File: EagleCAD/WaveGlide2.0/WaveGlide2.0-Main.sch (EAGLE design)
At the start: 47 parts, among them CN3 0, IC1 MC33502D, K2 MS-20-310-HN, Q2 reset, U1 ATMEGA328P_TQFP, U2 BMP180, U3 MPXV7002, U4 TPS55340PWP, U5 UG-2828GDEDF11, Y2 12MHz

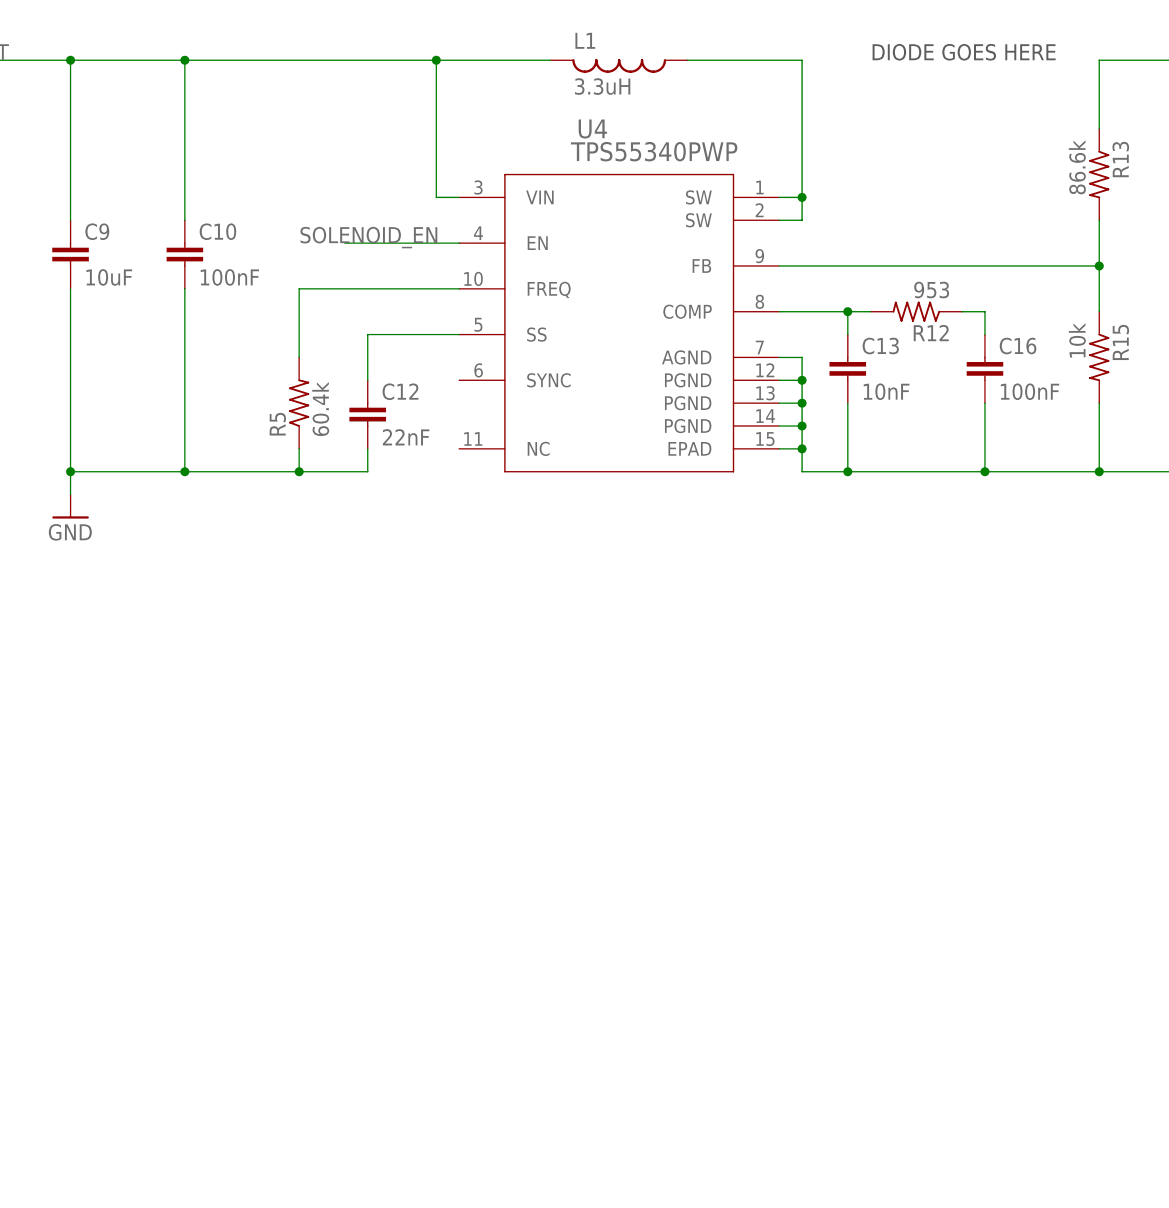
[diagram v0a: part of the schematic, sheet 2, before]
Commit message: Add 5V regulator
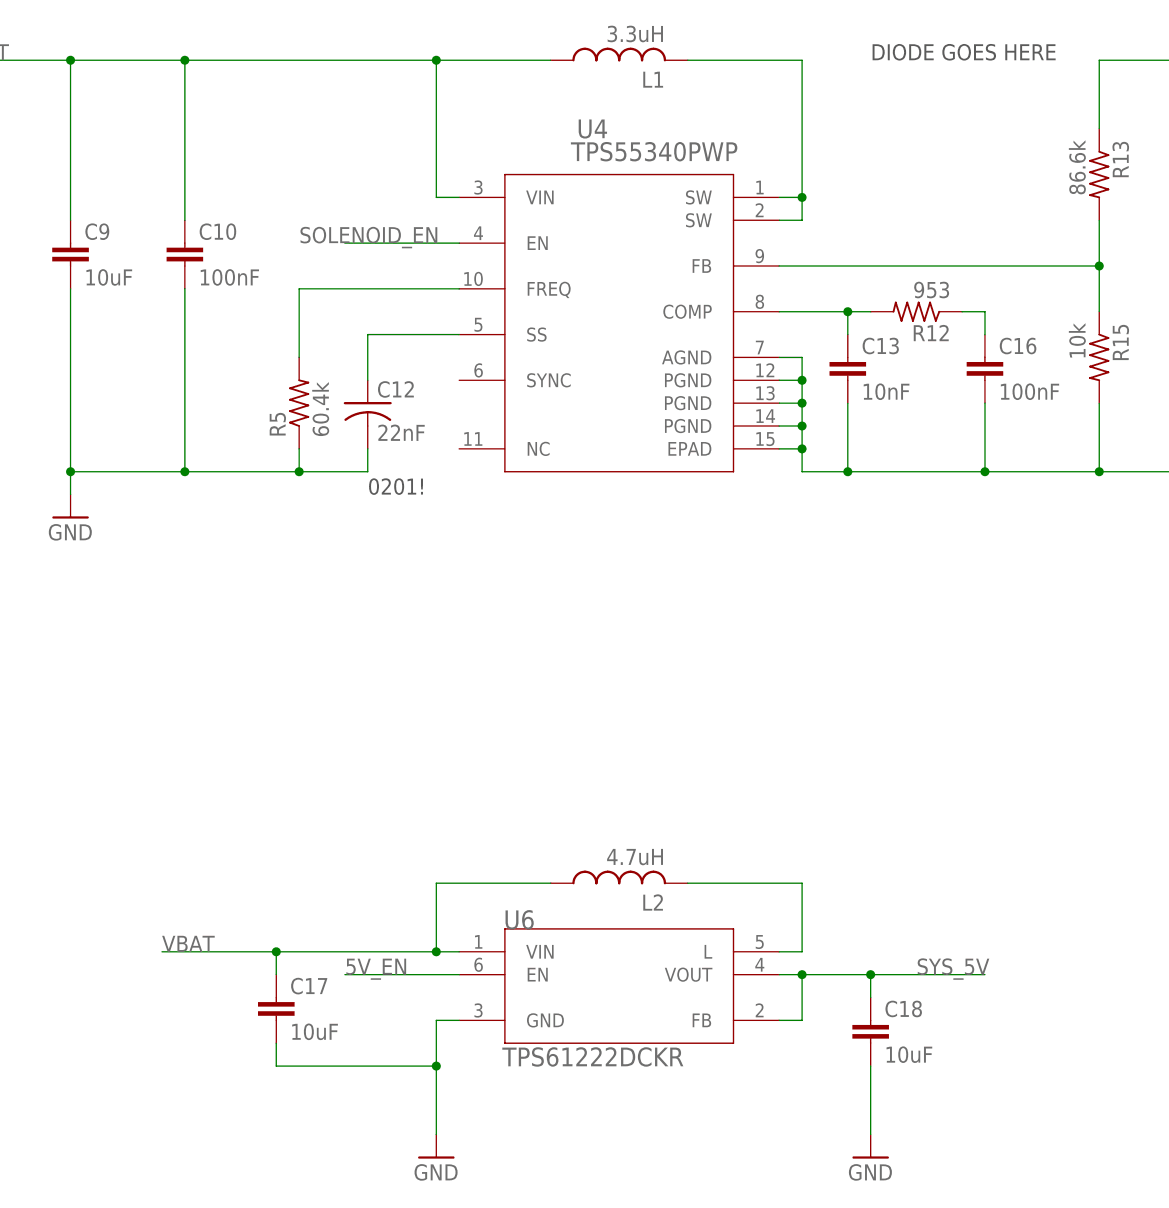
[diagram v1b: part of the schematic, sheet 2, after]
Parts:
- added C17, C18: 10uF, resistor:C-EUC0805
- added L2: 4.7uH, resistor:L-USL2825P
- added U6: TPS61222DCKR, CustomParts:TPS61222DCKR
- C12: device resistor:C-EUC0805 -> resistor:C-USC0201
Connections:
- new net 5V_EN: U6.EN
- new net N$6: L2.2, U6.L
- net GND: now also C17.2, C18.2, U6.GND
- net SYS_5V: now also C18.1, U6.FB, U6.VOUT
- net TPS55340_SW: now also L1.2; no longer L1.1
- net VBAT: now also C17.1, L1.1, L2.1, U6.VIN; no longer L1.2
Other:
- note added: "0201!"
- moved on the sheet: L1
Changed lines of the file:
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@@
 <?xml version="1.0" encoding="utf-8"?>
 <!DOCTYPE eagle SYSTEM "eagle.dtd">
-<eagle version="8.7.0">
+<eagle version="8.7.1">
 <drawing>
 <settings>
@@
 <attribute name="POPULATE" value="1"/>
 </part>
-<part name="C12" library="resistor" library_urn="urn:adsk.eagle:library:348" deviceset="C-EU" device="C0805" package3d_urn="urn:adsk.eagle:package:26137/1" value="22nF">
+<part name="C12" library="resistor" library_urn="urn:adsk.eagle:library:348" deviceset="C-US" device="C0201" package3d_urn="urn:adsk.eagle:package:26209/1" value="22nF">
 <attribute name="MPN" value="GRM033R60J223KE01D"/>
 <attribute name="POPULATE" value="1"/>
@@
 <attribute name="POPULATE" value="1"/>
 </part>
-<part name="U4" library="CustomParts" library_urn="urn:adsk.eagle:library:2193978" deviceset="TPS55340PWP" device="" package3d_urn="urn:adsk.eagle:package:2335473/2"/>
+<part name="U4" library="CustomParts" library_urn="urn:adsk.eagle:library:2193978" deviceset="TPS55340PWP" device="" package3d_urn="urn:adsk.eagle:package:2335473/3"/>
 <part name="GND7" library="supply1" library_urn="urn:adsk.eagle:library:371" deviceset="GND" device=""/>
 <part name="GND8" library="supply1" library_urn="urn:adsk.eagle:library:371" deviceset="GND" device=""/>
+<part name="U6" library="CustomParts" library_urn="urn:adsk.eagle:library:2193978" deviceset="TPS61222DCKR" device="" package3d_urn="urn:adsk.eagle:package:2230384/2">
+<attribute name="POPULATE" value="1"/>
+</part>
+<part name="L2" library="resistor" library_urn="urn:adsk.eagle:library:348" deviceset="L-US" device="L2825P" package3d_urn="urn:adsk.eagle:package:25928/1" value="4.7uH">
+<attribute name="MPN" value="LQM2HPN4R7MGCL"/>
+<attribute name="POPULATE" value="1"/>
+</part>
+<part name="C17" library="resistor" library_urn="urn:adsk.eagle:library:348" deviceset="C-EU" device="C0805" package3d_urn="urn:adsk.eagle:package:26137/1" value="10uF">
+<attribute name="MPN" value="GRM21BR60J106ME19L"/>
+<attribute name="POPULATE" value="1"/>
+<attribute name="TOL" value="20%"/>
+<attribute name="VOLT" value="6.3V"/>
+</part>
+<part name="C18" library="resistor" library_urn="urn:adsk.eagle:library:348" deviceset="C-EU" device="C0805" package3d_urn="urn:adsk.eagle:package:26137/1" value="10uF">
+<attribute name="MPN" value="C0805C106K8PACTU"/>
+<attribute name="POPULATE" value="1"/>
+<attribute name="TOL" value="10%"/>
+<attribute name="VOLT" value="10V"/>
+</part>
+<part name="GND9" library="supply1" library_urn="urn:adsk.eagle:library:371" deviceset="GND" device=""/>
+<part name="GND10" library="supply1" library_urn="urn:adsk.eagle:library:371" deviceset="GND" device=""/>
 </parts>
 <sheets>
@@
 <plain>
 <text x="121.92" y="254" size="1.778" layer="97">DIODE GOES HERE</text>
+<text x="66.04" y="205.74" size="1.778" layer="97">0201!</text>
 </plain>
 <instances>
@@
 <attribute name="POPULATE" x="147.32" y="220.98" size="1.778" layer="96" display="off"/>
 </instance>
-<instance part="L1" gate="G$1" x="93.98" y="254" rot="R270">
-<attribute name="MPN" x="93.98" y="254" size="1.778" layer="96" rot="R270" display="off"/>
-<attribute name="POPULATE" x="93.98" y="254" size="1.778" layer="96" display="off"/>
+<instance part="L1" gate="G$1" x="93.98" y="254" rot="R90">
+<attribute name="MPN" x="93.98" y="254" size="1.778" layer="96" rot="R90" display="off"/>
+<attribute name="POPULATE" x="93.98" y="254" size="1.778" layer="96" rot="R180" display="off"/>
 </instance>
 <instance part="U4" gate="A" x="93.98" y="226.06"/>
 <instance part="GND7" gate="1" x="33.02" y="203.2"/>
 <instance part="GND8" gate="1" x="170.18" y="203.2"/>
+<instance part="U6" gate="A" x="93.98" y="149.86">
+<attribute name="POPULATE" x="93.98" y="149.86" size="1.778" layer="96" display="off"/>
+</instance>
+<instance part="L2" gate="G$1" x="93.98" y="162.56" rot="R90">
+<attribute name="MPN" x="93.98" y="162.56" size="1.778" layer="96" rot="R90" display="off"/>
+<attribute name="POPULATE" x="93.98" y="162.56" size="1.778" layer="96" rot="R90" display="off"/>
+</instance>
+<instance part="C17" gate="G$1" x="55.88" y="149.86">
+<attribute name="MPN" x="55.88" y="149.86" size="1.778" layer="96" rot="R270" display="off"/>
+<attribute name="POPULATE" x="55.88" y="149.86" size="1.778" layer="96" display="off"/>
+<attribute name="VOLT" x="55.88" y="149.86" size="1.778" layer="96" display="off"/>
+<attribute name="TOL" x="55.88" y="149.86" size="1.778" layer="96" display="off"/>
+</instance>
+<instance part="C18" gate="G$1" x="121.92" y="147.32">
+<attribute name="MPN" x="121.92" y="147.32" size="1.778" layer="96" rot="R270" display="off"/>
+<attribute name="POPULATE" x="121.92" y="147.32" size="1.778" layer="96" display="off"/>
+<attribute name="VOLT" x="121.92" y="147.32" size="1.778" layer="96" display="off"/>
+</instance>
+<instance part="GND9" gate="1" x="73.66" y="132.08"/>
+<instance part="GND10" gate="1" x="121.92" y="132.08"/>
 </instances>
 <busses>
@@
 <segment>
 <pinref part="C9" gate="G$1" pin="1"/>
-<pinref part="L1" gate="G$1" pin="2"/>
-<wire x1="86.36" y1="254" x2="73.66" y2="254" width="0.1524" layer="91"/>
 <wire x1="73.66" y1="254" x2="45.72" y2="254" width="0.1524" layer="91"/>
 <wire x1="45.72" y1="254" x2="33.02" y2="254" width="0.1524" layer="91"/>
@@
 <wire x1="76.2" y1="238.76" x2="73.66" y2="238.76" width="0.1524" layer="91"/>
 <wire x1="73.66" y1="238.76" x2="73.66" y2="254" width="0.1524" layer="91"/>
-<junction x="73.66" y="254"/>
 <pinref part="C10" gate="G$1" pin="1"/>
 <wire x1="45.72" y1="236.22" x2="45.72" y2="254" width="0.1524" layer="91"/>
@@
 <junction x="33.02" y="254"/>
 <label x="20.32" y="254" size="1.778" layer="95"/>
+<pinref part="L1" gate="G$1" pin="1"/>
+<wire x1="73.66" y1="254" x2="86.36" y2="254" width="0.1524" layer="91"/>
+<junction x="73.66" y="254"/>
+</segment>
+<segment>
+<pinref part="C17" gate="G$1" pin="1"/>
+<wire x1="55.88" y1="152.4" x2="55.88" y2="154.94" width="0.1524" layer="91"/>
+<pinref part="U6" gate="A" pin="VIN"/>
+<wire x1="55.88" y1="154.94" x2="73.66" y2="154.94" width="0.1524" layer="91"/>
+<wire x1="73.66" y1="154.94" x2="76.2" y2="154.94" width="0.1524" layer="91"/>
+<junction x="73.66" y="154.94"/>
+<wire x1="73.66" y1="154.94" x2="73.66" y2="162.56" width="0.1524" layer="91"/>
+<wire x1="73.66" y1="162.56" x2="86.36" y2="162.56" width="0.1524" layer="91"/>
+<pinref part="L2" gate="G$1" pin="1"/>
+<wire x1="55.88" y1="154.94" x2="43.18" y2="154.94" width="0.1524" layer="91"/>
+<junction x="55.88" y="154.94"/>
+<label x="43.18" y="154.94" size="1.778" layer="95"/>
 </segment>
 </net>
@@
 <segment>
 <pinref part="U4" gate="A" pin="SW@2"/>
-<pinref part="L1" gate="G$1" pin="1"/>
-<wire x1="101.6" y1="254" x2="114.3" y2="254" width="0.1524" layer="91"/>
 <wire x1="114.3" y1="254" x2="114.3" y2="238.76" width="0.1524" layer="91"/>
 <wire x1="114.3" y1="238.76" x2="111.76" y2="238.76" width="0.1524" layer="91"/>
@@
 <pinref part="U4" gate="A" pin="SW@1"/>
 <wire x1="111.76" y1="236.22" x2="114.3" y2="236.22" width="0.1524" layer="91"/>
+<pinref part="L1" gate="G$1" pin="2"/>
+<wire x1="101.6" y1="254" x2="114.3" y2="254" width="0.1524" layer="91"/>
 </segment>
 </net>
@@
 <junction x="170.18" y="208.28"/>
 </segment>
-</net>
+<segment>
+<pinref part="GND9" gate="1" pin="GND"/>
+<pinref part="C17" gate="G$1" pin="2"/>
+<wire x1="73.66" y1="142.24" x2="73.66" y2="134.62" width="0.1524" layer="91"/>
+<wire x1="55.88" y1="144.78" x2="55.88" y2="142.24" width="0.1524" layer="91"/>
+<wire x1="55.88" y1="142.24" x2="73.66" y2="142.24" width="0.1524" layer="91"/>
+<pinref part="U6" gate="A" pin="GND"/>
+<wire x1="76.2" y1="147.32" x2="73.66" y2="147.32" width="0.1524" layer="91"/>
+<wire x1="73.66" y1="147.32" x2="73.66" y2="142.24" width="0.1524" layer="91"/>
+<junction x="73.66" y="142.24"/>
+</segment>
+<segment>
+<pinref part="C18" gate="G$1" pin="2"/>
+<pinref part="GND10" gate="1" pin="GND"/>
+<wire x1="121.92" y1="142.24" x2="121.92" y2="134.62" width="0.1524" layer="91"/>
+</segment>
+</net>
+<net name="N$6" class="0">
+<segment>
+<pinref part="L2" gate="G$1" pin="2"/>
+<wire x1="101.6" y1="162.56" x2="114.3" y2="162.56" width="0.1524" layer="91"/>
+<wire x1="114.3" y1="162.56" x2="114.3" y2="154.94" width="0.1524" layer="91"/>
+<pinref part="U6" gate="A" pin="L"/>
+<wire x1="114.3" y1="154.94" x2="111.76" y2="154.94" width="0.1524" layer="91"/>
+</segment>
+</net>
+<net name="SYS_5V" class="0">
+<segment>
+<pinref part="U6" gate="A" pin="VOUT"/>
+<wire x1="111.76" y1="152.4" x2="114.3" y2="152.4" width="0.1524" layer="91"/>
+<wire x1="114.3" y1="152.4" x2="121.92" y2="152.4" width="0.1524" layer="91"/>
+<wire x1="121.92" y1="152.4" x2="121.92" y2="149.86" width="0.1524" layer="91"/>
+<pinref part="C18" gate="G$1" pin="1"/>
+<pinref part="U6" gate="A" pin="FB"/>
+<wire x1="111.76" y1="147.32" x2="114.3" y2="147.32" width="0.1524" layer="91"/>
+<wire x1="114.3" y1="147.32" x2="114.3" y2="152.4" width="0.1524" layer="91"/>
+<junction x="114.3" y="152.4"/>
+<wire x1="121.92" y1="152.4" x2="134.62" y2="152.4" width="0.1524" layer="91"/>
+<junction x="121.92" y="152.4"/>
+<label x="127" y="152.4" size="1.778" layer="95"/>
+</segment>
+</net>
+<net name="5V_EN" class="0">
+<segment>
+<pinref part="U6" gate="A" pin="EN"/>
+<wire x1="76.2" y1="152.4" x2="63.5" y2="152.4" width="0.1524" layer="91"/>
+<label x="63.5" y="152.4" size="1.778" layer="95"/>
+</segment>
+</net>

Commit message: Add 13V boost for OLED
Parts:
- added C19: 4.7uF, resistor:C-EUC0603
- added C20: 47pF, resistor:C-EUC0603
- added C21: 1uF, resistor:C-EUC0805
- added L3: 18uH, resistor:L-USL4035M
- added R16: 1.5M, resistor:R-US_R0603
- added R17: 158k, resistor:R-US_R0603
- added U7: TPS61041DBVR, CustomParts:TPS61041DBVR
- L2: device resistor:L-USL2825P -> resistor:L-USL4035M
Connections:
- new net 13V_EN: U7.EN
- new net N$5: L3.2, U7.SW
- new net TPS55340_FB1: C20.2, R16.2, R17.1, U7.FB
- net GND: now also C19.2, C21.2, R17.2, U7.GND
- net SYS_13V: now also C20.1, C21.1, R16.1
- net VBAT: now also C19.1, L3.1, U7.VIN
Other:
- note added: "check package"

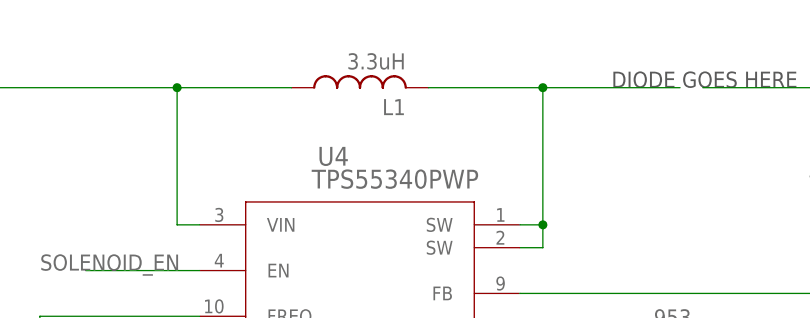
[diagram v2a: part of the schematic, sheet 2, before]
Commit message: Update BOM fix some bad components
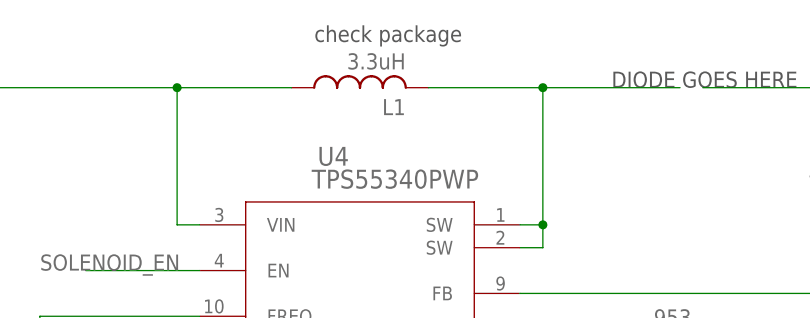
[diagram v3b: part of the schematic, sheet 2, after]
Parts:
- L1: TOL (none) -> 20%
- R12: MPN CRCW0402953RFKED -> CRCW0603953RFKEA; TOL (none) -> 1%
- R13: MPN CRCW040286K6FKED -> CRCW060386K6FKEA; TOL (none) -> 1%
- R15: device resistor:R-US_R0603 -> resistor:R-US_R0805; TOL (none) -> 0.5%
- R5: MPN CRCW040260K4FKED -> CRCW060360K4FKEA; TOL (none) -> 1%
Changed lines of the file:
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@@
 </part>
 <part name="R5" library="resistor" library_urn="urn:adsk.eagle:library:348" deviceset="R-US_" device="R0603" package3d_urn="urn:adsk.eagle:package:26057/1" value="60.4k">
-<attribute name="MPN" value="CRCW040260K4FKED"/>
-<attribute name="POPULATE" value="1"/>
+<attribute name="MPN" value="CRCW060360K4FKEA"/>
+<attribute name="POPULATE" value="1"/>
+<attribute name="TOL" value="1%"/>
 </part>
 <part name="R12" library="resistor" library_urn="urn:adsk.eagle:library:348" deviceset="R-US_" device="R0603" package3d_urn="urn:adsk.eagle:package:26057/1" value="953">
-<attribute name="MPN" value="CRCW0402953RFKED"/>
-<attribute name="POPULATE" value="1"/>
+<attribute name="MPN" value="CRCW0603953RFKEA"/>
+<attribute name="POPULATE" value="1"/>
+<attribute name="TOL" value="1%"/>
 </part>
 <part name="R13" library="resistor" library_urn="urn:adsk.eagle:library:348" deviceset="R-US_" device="R0603" package3d_urn="urn:adsk.eagle:package:26057/1" value="86.6k">
-<attribute name="MPN" value="CRCW040286K6FKED"/>
-<attribute name="POPULATE" value="1"/>
-</part>
-<part name="R15" library="resistor" library_urn="urn:adsk.eagle:library:348" deviceset="R-US_" device="R0603" package3d_urn="urn:adsk.eagle:package:26057/1" value="10k">
+<attribute name="MPN" value="CRCW060386K6FKEA"/>
+<attribute name="POPULATE" value="1"/>
+<attribute name="TOL" value="1%"/>
+</part>
+<part name="R15" library="resistor" library_urn="urn:adsk.eagle:library:348" deviceset="R-US_" device="R0805" package3d_urn="urn:adsk.eagle:package:26059/1" value="10k">
 <attribute name="MPN" value="RR1220P-103-D"/>
 <attribute name="POPULATE" value="1"/>
+<attribute name="TOL" value="0.5%"/>
 </part>
 <part name="L1" library="resistor" library_urn="urn:adsk.eagle:library:348" deviceset="L-US" device="L4532P" package3d_urn="urn:adsk.eagle:package:25935/1" value="3.3uH">
 <attribute name="MPN" value="XAL5030-332MEB"/>
 <attribute name="POPULATE" value="1"/>
+<attribute name="TOL" value="20%"/>
 </part>
 <part name="U4" library="CustomParts" library_urn="urn:adsk.eagle:library:2193978" deviceset="TPS55340PWP" device="" package3d_urn="urn:adsk.eagle:package:2335473/3"/>
@@
 <text x="86.36" y="167.64" size="1.778" layer="97">check package</text>
 <text x="116.84" y="109.22" size="1.778" layer="97">DIODE GOES HERE</text>
+<text x="88.9" y="259.08" size="1.778" layer="97">check package</text>
 </plain>
 <instances>
@@
 <attribute name="MPN" x="58.42" y="215.9" size="1.778" layer="96" rot="R270" display="off"/>
 <attribute name="POPULATE" x="58.42" y="215.9" size="1.778" layer="96" display="off"/>
+<attribute name="TOL" x="58.42" y="215.9" size="1.778" layer="96" rot="R90" display="off"/>
 </instance>
 <instance part="R12" gate="G$1" x="127" y="226.06" rot="R180">
 <attribute name="MPN" x="127" y="226.06" size="1.778" layer="96" rot="R270" display="off"/>
 <attribute name="POPULATE" x="127" y="226.06" size="1.778" layer="96" display="off"/>
+<attribute name="TOL" x="127" y="226.06" size="1.778" layer="96" rot="R180" display="off"/>
 </instance>
 <instance part="R13" gate="G$1" x="147.32" y="241.3" rot="R270">
 <attribute name="MPN" x="147.32" y="241.3" size="1.778" layer="96" rot="R270" display="off"/>
 <attribute name="POPULATE" x="147.32" y="241.3" size="1.778" layer="96" display="off"/>
+<attribute name="TOL" x="147.32" y="241.3" size="1.778" layer="96" rot="R270" display="off"/>
 </instance>
 <instance part="R15" gate="G$1" x="147.32" y="220.98" rot="R270">
 <attribute name="MPN" x="147.32" y="220.98" size="1.778" layer="96" rot="R270" display="off"/>
 <attribute name="POPULATE" x="147.32" y="220.98" size="1.778" layer="96" display="off"/>
+<attribute name="TOL" x="147.32" y="220.98" size="1.778" layer="96" display="off"/>
 </instance>
 <instance part="L1" gate="G$1" x="93.98" y="254" rot="R90">
 <attribute name="MPN" x="93.98" y="254" size="1.778" layer="96" rot="R90" display="off"/>
 <attribute name="POPULATE" x="93.98" y="254" size="1.778" layer="96" rot="R180" display="off"/>
+<attribute name="TOL" x="93.98" y="254" size="1.778" layer="96" rot="R90" display="off"/>
 </instance>
 <instance part="U4" gate="A" x="93.98" y="226.06"/>
